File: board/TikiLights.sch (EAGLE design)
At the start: 57 parts, among them IC1 AZ1117EH-3.3TRG1, SW3 ENCODER_SW1-PEC12, SW4 ENCODER_SW1-PEC12, U1 AZ1117E

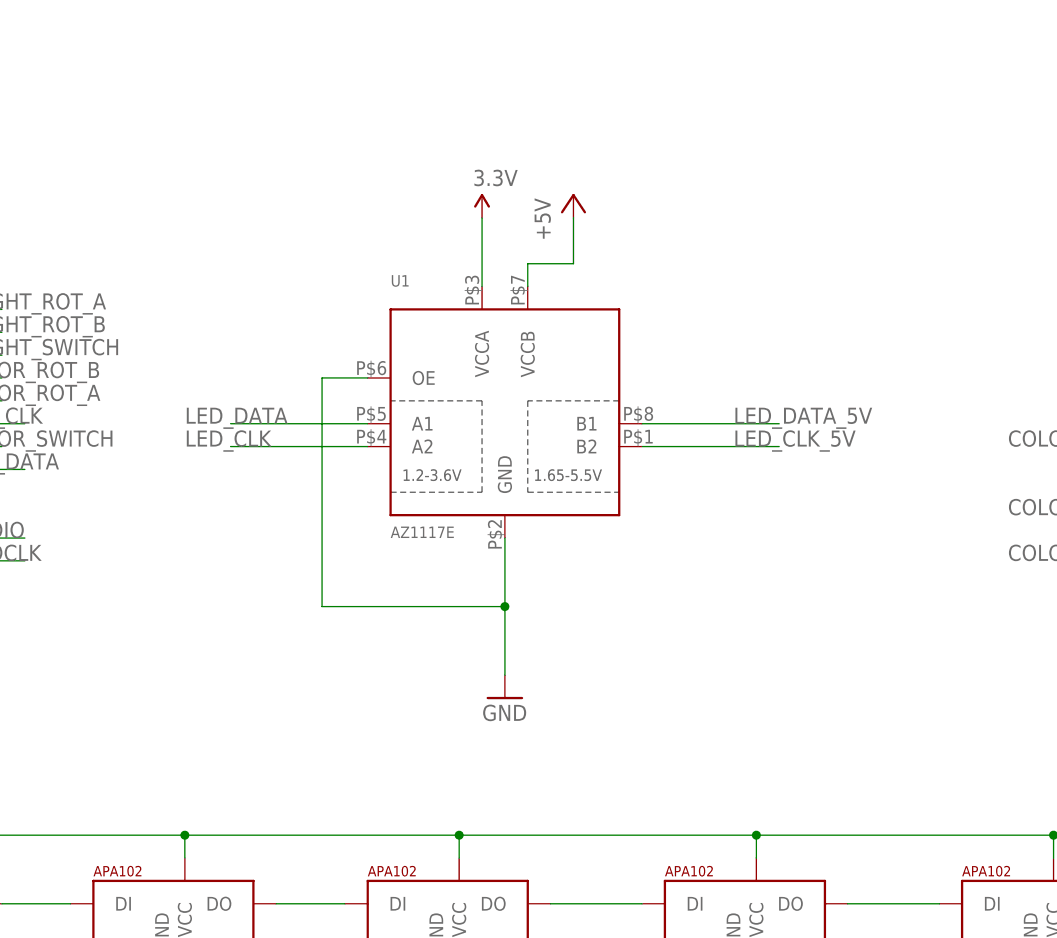
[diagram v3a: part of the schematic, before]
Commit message: Revision 2. Fixing TXB0102 board. Widening encoder side drill holes.
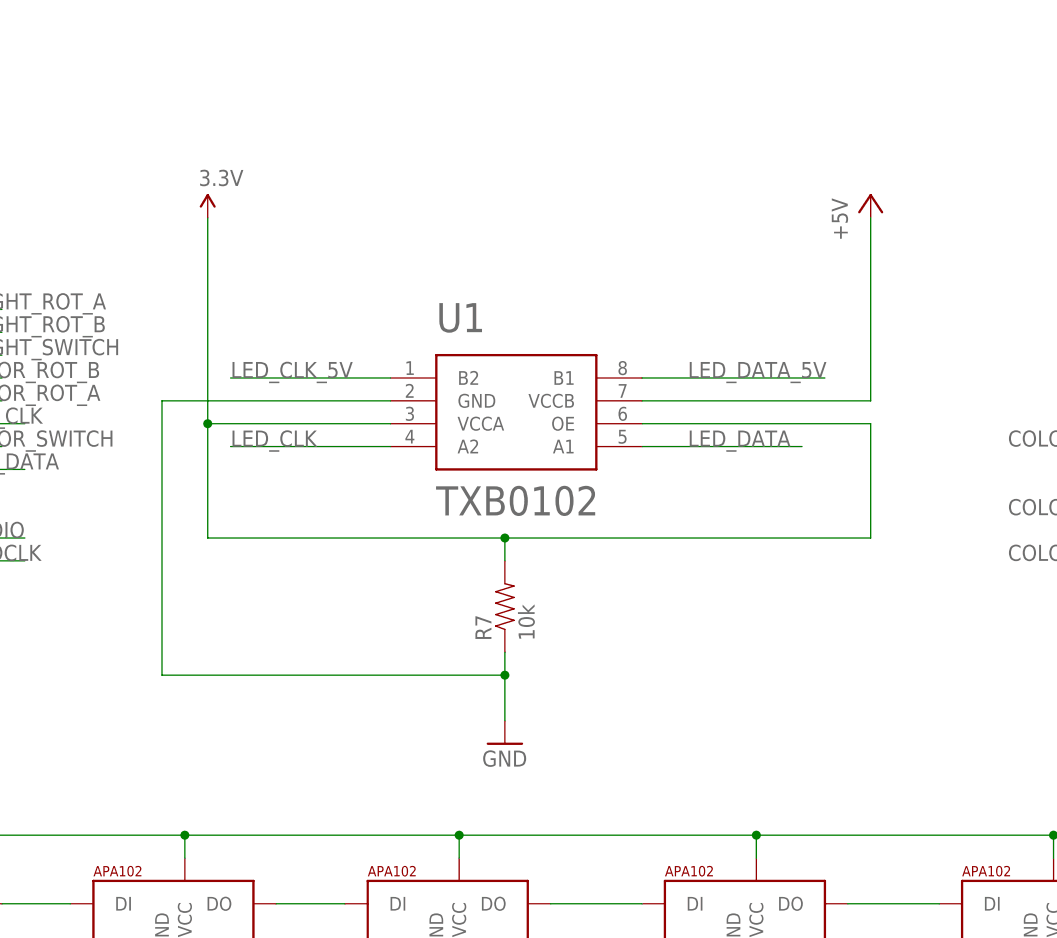
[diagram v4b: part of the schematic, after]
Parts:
- added R7: 10k, SparkFun-Resistors:RESISTOR0603
- U1: value AZ1117E -> TXB0102; device adafruit:TXS0102 -> TXB0102:TXB0102
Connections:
- net 3.3V: now also R7.2, U1.OE
- net GND: now also R7.1; no longer U1.OE
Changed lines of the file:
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@@
 <part name="P+6" library="supply1" deviceset="+5V" device=""/>
 <part name="GND9" library="supply1" deviceset="GND" device=""/>
-<part name="U1" library="adafruit" deviceset="TXS0102" device="" value="AZ1117E"/>
+<part name="U1" library="TXB0102" deviceset="TXB0102" device="" value="TXB0102"/>
 <part name="SUPPLY5" library="SparkFun-Aesthetics" deviceset="3.3V" device=""/>
 <part name="P+7" library="supply1" deviceset="+5V" device=""/>
@@
 <part name="C12" library="passives" deviceset="CAPACITOR" device="0603_CAP" value="0.1µF"/>
 <part name="C13" library="passives" deviceset="CAPACITOR" device="0603_CAP" value="0.1µF"/>
+<part name="R7" library="SparkFun-Resistors" deviceset="RESISTOR" device="0603" value="10k"/>
 </parts>
 <sheets>
@@
 <instance part="GND9" gate="1" x="48.26" y="15.24"/>
 <instance part="U1" gate="G$1" x="182.88" y="165.1"/>
-<instance part="SUPPLY5" gate="G$1" x="180.34" y="185.42"/>
-<instance part="P+7" gate="1" x="190.5" y="187.96"/>
-<instance part="GND10" gate="1" x="182.88" y="132.08"/>
+<instance part="SUPPLY5" gate="G$1" x="149.86" y="185.42"/>
+<instance part="P+7" gate="1" x="223.52" y="187.96"/>
+<instance part="GND10" gate="1" x="182.88" y="127"/>
 <instance part="SUPPLY6" gate="G$1" x="307.34" y="243.84"/>
 <instance part="GND11" gate="1" x="307.34" y="193.04"/>
@@
 <instance part="C12" gate="G$1" x="271.78" y="142.24"/>
 <instance part="C13" gate="G$1" x="281.94" y="142.24"/>
+<instance part="R7" gate="G$1" x="182.88" y="142.24" rot="R90"/>
 </instances>
 <busses>
@@
 <segment>
 <pinref part="P+7" gate="1" pin="+5V"/>
-<wire x1="190.5" y1="185.42" x2="190.5" y2="180.34" width="0.1524" layer="91"/>
-<wire x1="190.5" y1="180.34" x2="185.42" y2="180.34" width="0.1524" layer="91"/>
+<wire x1="223.52" y1="185.42" x2="223.52" y2="165.1" width="0.1524" layer="91"/>
+<wire x1="223.52" y1="165.1" x2="198.12" y2="165.1" width="0.1524" layer="91"/>
 <pinref part="U1" gate="G$1" pin="VCCB"/>
-<wire x1="185.42" y1="180.34" x2="185.42" y2="177.8" width="0.1524" layer="91"/>
 </segment>
 </net>
@@
 </segment>
 <segment>
-<pinref part="GND10" gate="1" pin="GND"/>
-<pinref part="U1" gate="G$1" pin="GND"/>
-<wire x1="182.88" y1="134.62" x2="182.88" y2="142.24" width="0.1524" layer="91"/>
-<pinref part="U1" gate="G$1" pin="OE"/>
-<wire x1="182.88" y1="142.24" x2="182.88" y2="149.86" width="0.1524" layer="91"/>
-<wire x1="167.64" y1="167.64" x2="162.56" y2="167.64" width="0.1524" layer="91"/>
-<wire x1="162.56" y1="167.64" x2="162.56" y2="142.24" width="0.1524" layer="91"/>
-<wire x1="162.56" y1="142.24" x2="182.88" y2="142.24" width="0.1524" layer="91"/>
-<junction x="182.88" y="142.24"/>
-</segment>
-<segment>
 <pinref part="U$7" gate="G$1" pin="GND"/>
 <pinref part="GND8" gate="1" pin="GND"/>
@@
 <junction x="271.78" y="132.08"/>
 </segment>
+<segment>
+<pinref part="R7" gate="G$1" pin="1"/>
+<pinref part="GND10" gate="1" pin="GND"/>
+<wire x1="182.88" y1="137.16" x2="182.88" y2="134.62" width="0.1524" layer="91"/>
+<pinref part="U1" gate="G$1" pin="GND"/>
+<wire x1="182.88" y1="134.62" x2="182.88" y2="129.54" width="0.1524" layer="91"/>
+<wire x1="170.18" y1="165.1" x2="144.78" y2="165.1" width="0.1524" layer="91"/>
+<wire x1="144.78" y1="165.1" x2="144.78" y2="134.62" width="0.1524" layer="91"/>
+<wire x1="144.78" y1="134.62" x2="182.88" y2="134.62" width="0.1524" layer="91"/>
+<junction x="182.88" y="134.62"/>
+</segment>
 </net>
 <net name="3.3V" class="0">
@@
 </segment>
 <segment>
-<pinref part="SUPPLY5" gate="G$1" pin="3.3V"/>
-<pinref part="U1" gate="G$1" pin="VCCA"/>
-<wire x1="180.34" y1="185.42" x2="180.34" y2="177.8" width="0.1524" layer="91"/>
-</segment>
-<segment>
 <pinref part="SW3" gate="SW" pin="2"/>
 <pinref part="SUPPLY6" gate="G$1" pin="3.3V"/>
@@
 <junction x="294.64" y="175.26"/>
 </segment>
+<segment>
+<pinref part="U1" gate="G$1" pin="VCCA"/>
+<pinref part="SUPPLY5" gate="G$1" pin="3.3V"/>
+<wire x1="170.18" y1="162.56" x2="149.86" y2="162.56" width="0.1524" layer="91"/>
+<wire x1="149.86" y1="162.56" x2="149.86" y2="185.42" width="0.1524" layer="91"/>
+<pinref part="U1" gate="G$1" pin="OE"/>
+<wire x1="198.12" y1="162.56" x2="223.52" y2="162.56" width="0.1524" layer="91"/>
+<wire x1="223.52" y1="162.56" x2="223.52" y2="149.86" width="0.1524" layer="91"/>
+<wire x1="223.52" y1="149.86" x2="182.88" y2="149.86" width="0.1524" layer="91"/>
+<wire x1="182.88" y1="149.86" x2="182.88" y2="147.32" width="0.1524" layer="91"/>
+<pinref part="R7" gate="G$1" pin="2"/>
+<wire x1="182.88" y1="149.86" x2="149.86" y2="149.86" width="0.1524" layer="91"/>
+<wire x1="149.86" y1="149.86" x2="149.86" y2="162.56" width="0.1524" layer="91"/>
+<junction x="182.88" y="149.86"/>
+<junction x="149.86" y="162.56"/>
+</segment>
 </net>
 <net name="SWDCLK" class="0">
@@
 <segment>
 <pinref part="U1" gate="G$1" pin="A1"/>
-<wire x1="167.64" y1="162.56" x2="152.4" y2="162.56" width="0.1524" layer="91"/>
-<label x="147.32" y="162.56" size="1.778" layer="95"/>
+<wire x1="198.12" y1="160.02" x2="215.9" y2="160.02" width="0.1524" layer="91"/>
+<label x="203.2" y="160.02" size="1.778" layer="95"/>
 </segment>
 </net>
@@
 <segment>
 <pinref part="U1" gate="G$1" pin="A2"/>
-<wire x1="167.64" y1="160.02" x2="152.4" y2="160.02" width="0.1524" layer="91"/>
-<label x="147.32" y="160.02" size="1.778" layer="95"/>
+<wire x1="170.18" y1="160.02" x2="152.4" y2="160.02" width="0.1524" layer="91"/>
+<label x="152.4" y="160.02" size="1.778" layer="95"/>
 </segment>
 </net>
@@
 <segment>
 <pinref part="U1" gate="G$1" pin="B2"/>
-<wire x1="198.12" y1="160.02" x2="213.36" y2="160.02" width="0.1524" layer="91"/>
-<label x="208.28" y="160.02" size="1.778" layer="95"/>
+<wire x1="170.18" y1="167.64" x2="152.4" y2="167.64" width="0.1524" layer="91"/>
+<label x="152.4" y="167.64" size="1.778" layer="95"/>
 </segment>
 <segment>
@@
 <segment>
 <pinref part="U1" gate="G$1" pin="B1"/>
-<wire x1="198.12" y1="162.56" x2="213.36" y2="162.56" width="0.1524" layer="91"/>
-<label x="208.28" y="162.56" size="1.778" layer="95"/>
-</segment>
-<segment>
+<wire x1="198.12" y1="167.64" x2="218.44" y2="167.64" width="0.1524" layer="91"/>
+<label x="203.2" y="167.64" size="1.778" layer="95"/>
+</segment>
+<segment>
